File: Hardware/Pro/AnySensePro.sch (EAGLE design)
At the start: 45 parts, among them U1 LP2992IM5-3.3, U3 SN65HVD232D, U4 STM32F303RET6, U6 M25P16VMN6P, X6 MEM2051-00-195-00-A, X7 TC2030-IDC-NL, Y1 ABM3B

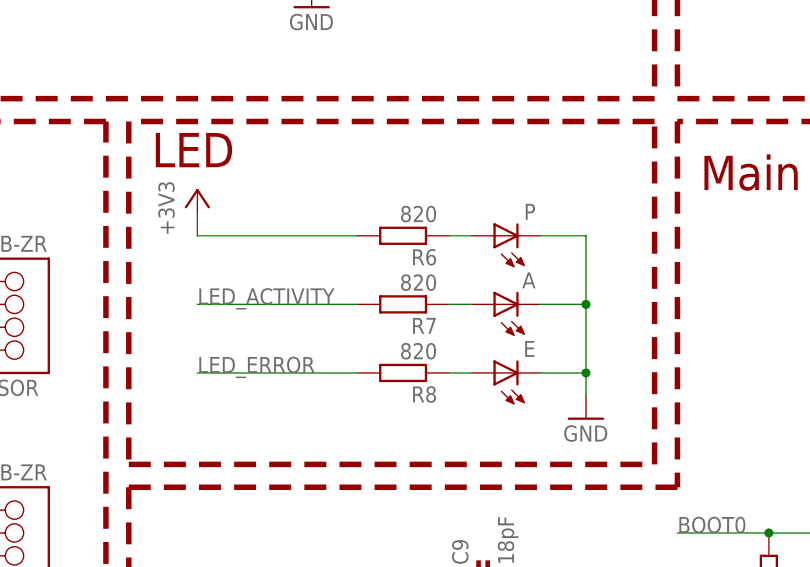
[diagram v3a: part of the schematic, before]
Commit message: Farnell OC's updated and paste pad reduction removed.
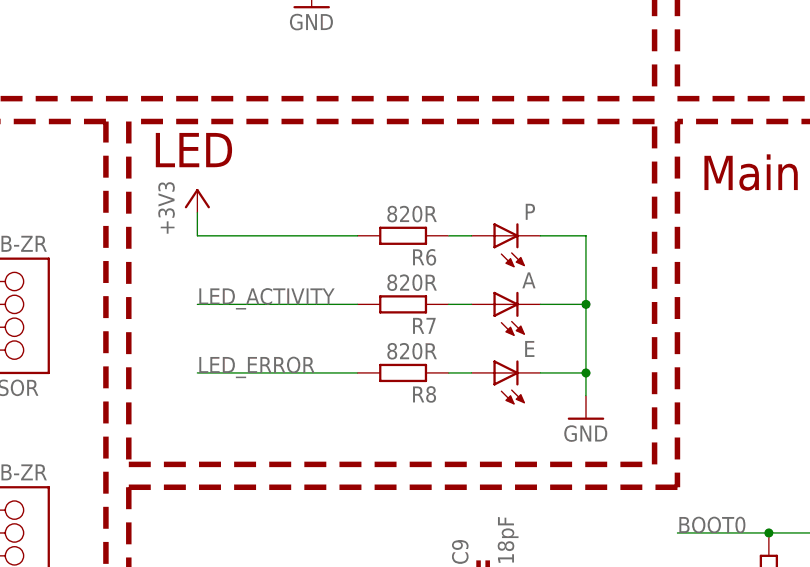
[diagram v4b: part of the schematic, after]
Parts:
- R1, R11: OC_FARNELL 2302739RL -> 2302453RL
- R13: OC_FARNELL 2302739RL -> 2302754RL
- R4: OC_FARNELL 2302739RL -> 2302656RL
- R6, R7, R8: value 820 -> 820R
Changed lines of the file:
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@@
 <attribute name="OC_FARNELL" value="2468792RL"/>
 </part>
-<part name="R6" library="rcl" deviceset="R-EU_" device="R0402" value="820">
+<part name="R6" library="rcl" deviceset="R-EU_" device="R0402" value="820R">
 <attribute name="OC_FARNELL" value="2302628RL"/>
 </part>
-<part name="R7" library="rcl" deviceset="R-EU_" device="R0402" value="820">
+<part name="R7" library="rcl" deviceset="R-EU_" device="R0402" value="820R">
 <attribute name="OC_FARNELL" value="2302628RL"/>
 </part>
-<part name="R8" library="rcl" deviceset="R-EU_" device="R0402" value="820">
+<part name="R8" library="rcl" deviceset="R-EU_" device="R0402" value="820R">
 <attribute name="OC_FARNELL" value="2302628RL"/>
 </part>
 <part name="+3V38" library="supply1" deviceset="+3V3" device=""/>
 <part name="R4" library="rcl" deviceset="R-EU_" device="R0402" value="1.5K">
-<attribute name="OC_FARNELL" value="2302739RL"/>
+<attribute name="OC_FARNELL" value="2302656RL"/>
 </part>
 <part name="R1" library="rcl" deviceset="R-EU_" device="R0402" value="22R">
-<attribute name="OC_FARNELL" value="2302739RL"/>
+<attribute name="OC_FARNELL" value="2302453RL"/>
 </part>
 <part name="R11" library="rcl" deviceset="R-EU_" device="R0402" value="22R">
-<attribute name="OC_FARNELL" value="2302739RL"/>
+<attribute name="OC_FARNELL" value="2302453RL"/>
 </part>
 <part name="R12" library="rcl" deviceset="R-EU_" device="R0402" value="10K">
@@
 </part>
 <part name="R13" library="rcl" deviceset="R-EU_" device="R0402" value="15K">
-<attribute name="OC_FARNELL" value="2302739RL"/>
+<attribute name="OC_FARNELL" value="2302754RL"/>
 </part>
 <part name="GND2" library="supply1" deviceset="GND" device=""/>
